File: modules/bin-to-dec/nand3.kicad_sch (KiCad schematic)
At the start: 8 parts, among them Q1 DMP3099L, Q2 DMP3099L, Q3 2N7002, Q4 2N7002, Q5 2N7002, Q6 2N7002, Q7 DMP3099L, Q8 DMP3099L

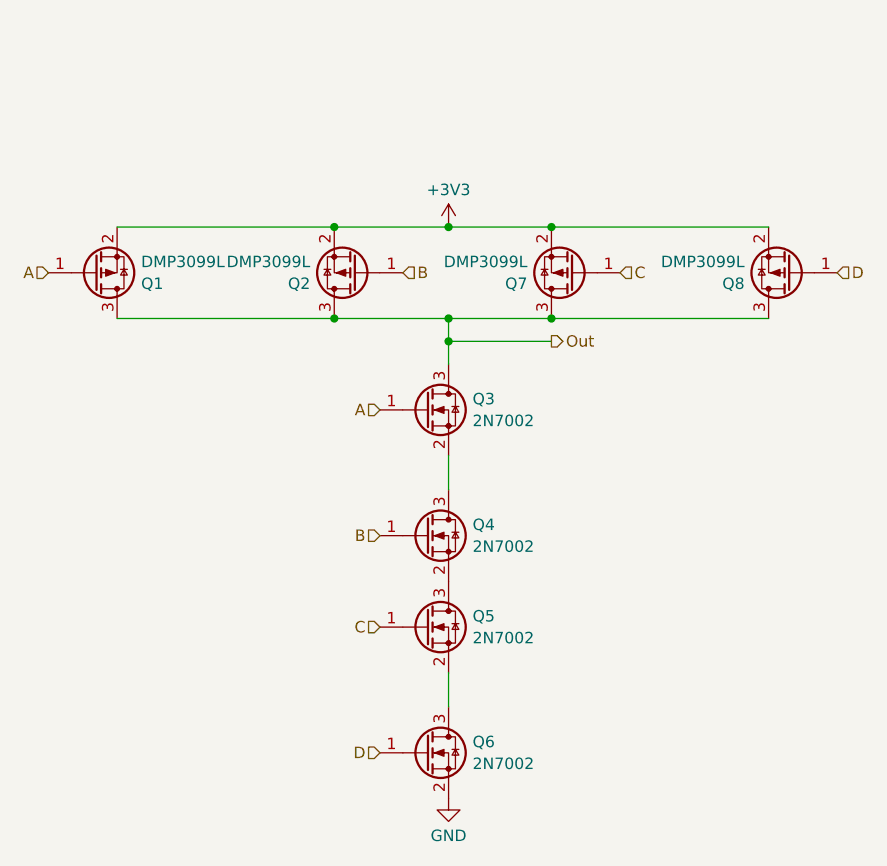
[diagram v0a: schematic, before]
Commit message: move to correct dir. improved symmetry of pcb
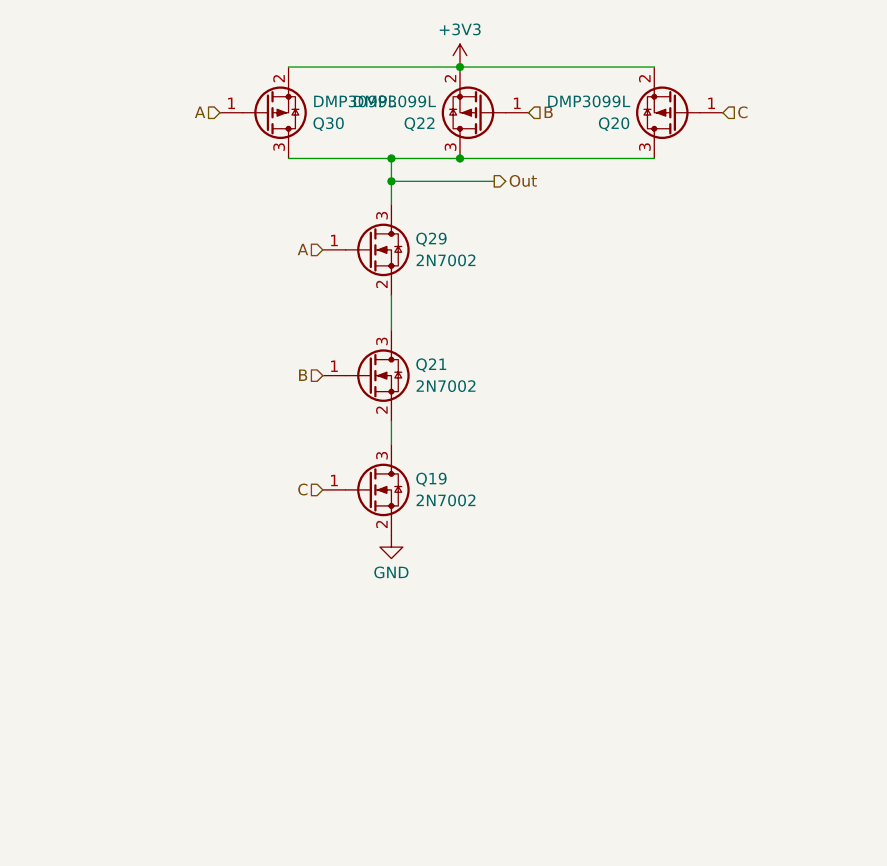
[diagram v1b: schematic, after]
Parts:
- removed Q1, Q2, Q7, Q8: DMP3099L, Package_TO_SOT_SMD:SOT-23, symbol Transistor_FET:DMP3099L
- removed Q3, Q4, Q5, Q6: 2N7002, Package_TO_SOT_SMD:SOT-23, symbol Transistor_FET:2N7002
- added Q19, Q21, Q29: 2N7002, Package_TO_SOT_SMD:SOT-23, symbol Transistor_FET:2N7002
- added Q20, Q22, Q30: DMP3099L, Package_TO_SOT_SMD:SOT-23, symbol Transistor_FET:DMP3099L
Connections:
- net +3V3: now also Q20.2 (S), Q22.2 (S), Q30.2 (S)
- net A: now also Q29.1 (G), Q30.1 (G)
- net B: now also Q21.1 (G), Q22.1 (G)
- net C: now also Q19.1 (G), Q20.1 (G)
- net GND: now also Q19.2 (S)
- net Out: now also Q20.3 (D), Q22.3 (D), Q29.3 (D), Q30.3 (D)
- new net: Q21.3 (D), Q29.2 (S)
- new net: Q19.3 (D), Q21.2 (S)

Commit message: using plugin to generate jlc production files
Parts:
- Q19, Q21, Q29: LCSC Part # (none) -> C8545
- Q20, Q22, Q30: LCSC Part # (none) -> C2940610
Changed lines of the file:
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@@
+			)
+		)
+		(property "LCSC Part #" "C8545"
+			(at 135.89 69.85 0)
+			(effects
+				(font
+					(size 1.27 1.27)
+				)
+				(hide yes)
 			)
 		)
@@
 			)
 		)
+		(property "LCSC Part #" "C8545"
+			(at 135.89 83.82 0)
+			(effects
+				(font
+					(size 1.27 1.27)
+				)
+				(hide yes)
+			)
+		)
 		(pin "1"
 		)
@@
 			)
 		)
+		(property "LCSC Part #" "C8545"
+			(at 135.89 96.52 0)
+			(effects
+				(font
+					(size 1.27 1.27)
+				)
+				(hide yes)
+			)
+		)
 		(pin "1"
 		)
@@
 			)
 		)
+		(property "LCSC Part #" "C2940610"
+			(at 124.46 54.61 0)
+			(effects
+				(font
+					(size 1.27 1.27)
+				)
+				(hide yes)
+			)
+		)
 		(pin "2"
 		)
@@
 			)
 		)
+		(property "LCSC Part #" "C2940610"
+			(at 170.18 54.61 0)
+			(effects
+				(font
+					(size 1.27 1.27)
+				)
+				(hide yes)
+			)
+		)
 		(pin "2"
 		)
@@
 			(at 148.59 54.61 0)
 			(effects
+				(font
+					(size 1.27 1.27)
+				)
+				(hide yes)
+			)
+		)
+		(property "LCSC Part #" "C2940610"
+			(at 148.59 54.61 0)
+			(effects

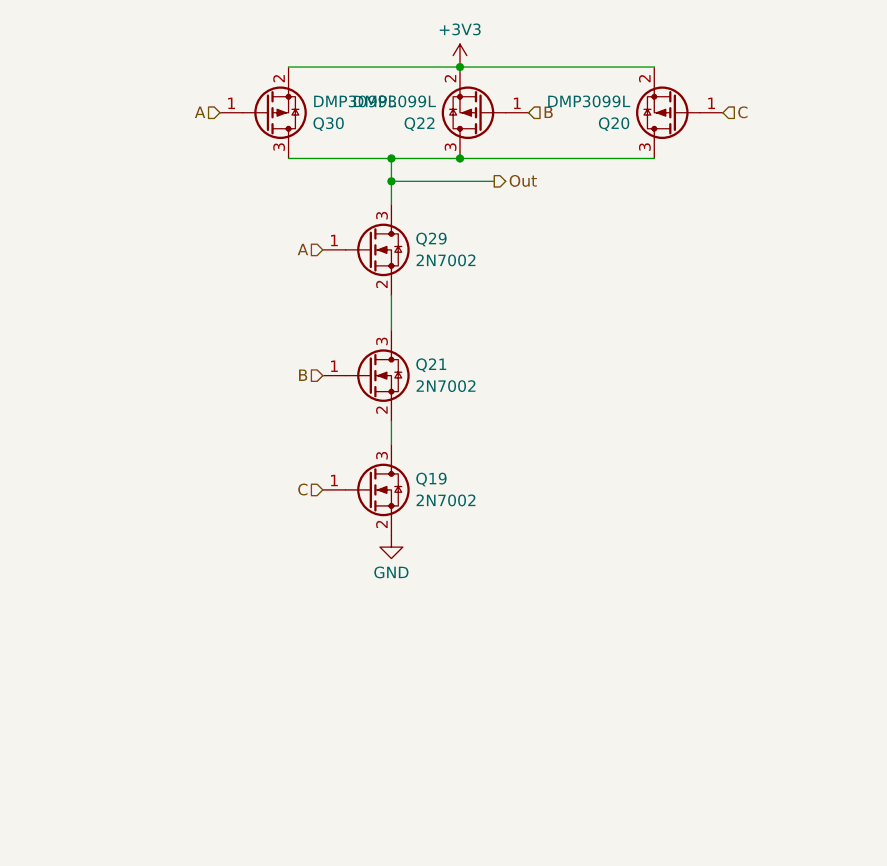
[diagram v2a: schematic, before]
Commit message: move components to top layer :(
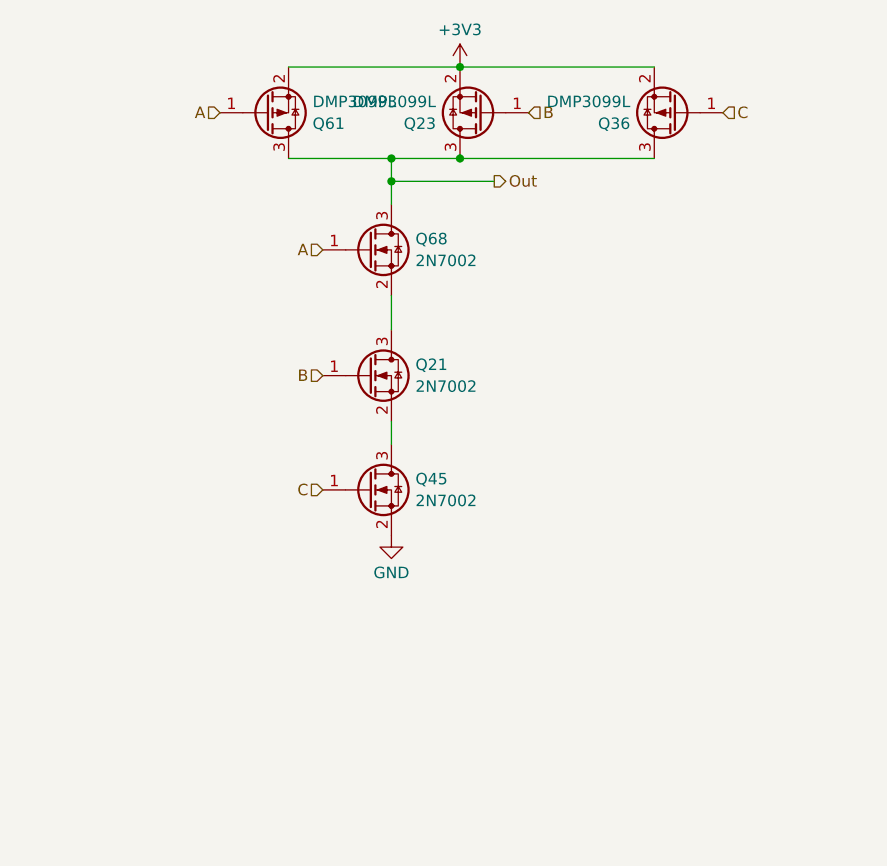
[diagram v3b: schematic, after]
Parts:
- Q21: LCSC part number (none) -> C8545
- Q23: renamed from Q22; LCSC part number (none) -> C2940610
- Q36: renamed from Q20; LCSC part number (none) -> C2940610
- Q45: renamed from Q19; LCSC part number (none) -> C8545
- Q61: renamed from Q30; LCSC part number (none) -> C2940610
- Q68: renamed from Q29; LCSC part number (none) -> C8545

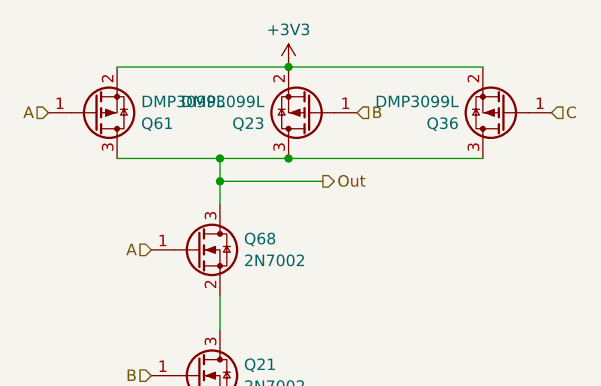
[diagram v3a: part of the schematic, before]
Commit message: switched to jlc basic components
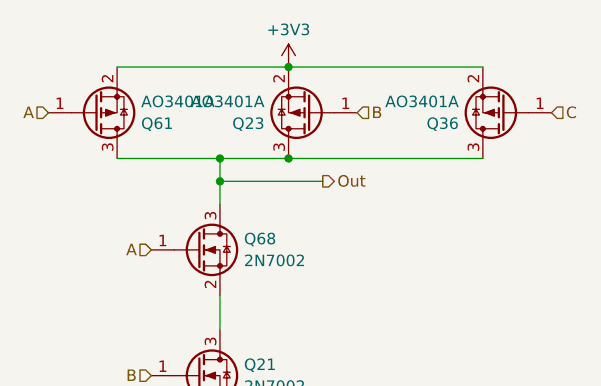
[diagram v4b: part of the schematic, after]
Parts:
- Q23, Q36, Q61: value DMP3099L -> AO3401A; LCSC Part # C2940610 -> C15127
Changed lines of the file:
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@@
 			)
 		)
-		(property "Value" "DMP3099L"
+		(property "Value" "AO3401A"
 			(at 129.667 53.3979 0)
 			(effects
@@
 			)
 		)
-		(property "Datasheet" "https://www.diodes.com/assets/Datasheets/DMP3099L.pdf"
+		(property "Datasheet" "https://jlcpcb.com/api/file/downloadByFileSystemAccessId/8553305450243108864"
 			(at 129.54 50.8 0)
 			(effects
@@
 			)
 		)
-		(property "LCSC Part #" "C2940610"
+		(property "LCSC Part #" "C15127"
 			(at 124.46 54.61 0)
 			(effects
@@
 			)
 		)
-		(property "Value" "DMP3099L"
+		(property "Value" "AO3401A"
 			(at 164.973 53.3979 0)
 			(effects
@@
 			)
 		)
-		(property "Datasheet" "https://www.diodes.com/assets/Datasheets/DMP3099L.pdf"
+		(property "Datasheet" "https://jlcpcb.com/api/file/downloadByFileSystemAccessId/8553305450243108864"
 			(at 165.1 50.8 0)
 			(effects
@@
 			)
 		)
-		(property "LCSC Part #" "C2940610"
+		(property "LCSC Part #" "C15127"
 			(at 170.18 54.61 0)
 			(effects
@@
 			)
 		)
-		(property "Value" "DMP3099L"
+		(property "Value" "AO3401A"
 			(at 143.383 53.3979 0)
 			(effects
@@
 			)
 		)
-		(property "Datasheet" "https://www.diodes.com/assets/Datasheets/DMP3099L.pdf"
+		(property "Datasheet" "https://jlcpcb.com/api/file/downloadByFileSystemAccessId/8553305450243108864"
 			(at 143.51 50.8 0)
 			(effects
@@
 			)
 		)
-		(property "LCSC Part #" "C2940610"
+		(property "LCSC Part #" "C15127"
 			(at 148.59 54.61 0)
 			(effects

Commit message: minor edits
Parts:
- Q21, Q45, Q68: LCSC part number C8545 -> (none)
- Q23, Q36, Q61: LCSC part number C2940610 -> (none)
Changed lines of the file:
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@@
-			)
-		)
-		(property "LCSC part number" "C8545"
-			(at 135.89 69.85 0)
-			(effects
-				(font
-					(size 1.27 1.27)
-				)
-				(hide yes)
 			)
 		)
@@
 			)
 		)
-		(property "LCSC part number" "C8545"
-			(at 135.89 83.82 0)
-			(effects
-				(font
-					(size 1.27 1.27)
-				)
-				(hide yes)
-			)
-		)
 		(pin "1"
 		)
@@
 			)
 		)
-		(property "LCSC part number" "C8545"
-			(at 135.89 96.52 0)
-			(effects
-				(font
-					(size 1.27 1.27)
-				)
-				(hide yes)
-			)
-		)
 		(pin "1"
 		)
@@
 			)
 		)
-		(property "LCSC part number" "C2940610"
-			(at 124.46 54.61 0)
-			(effects
-				(font
-					(size 1.27 1.27)
-				)
-				(hide yes)
-			)
-		)
 		(pin "2"
 		)
@@
 			)
 		)
-		(property "LCSC part number" "C2940610"
-			(at 170.18 54.61 0)
-			(effects
-				(font
-					(size 1.27 1.27)
-				)
-				(hide yes)
-			)
-		)
 		(pin "2"
 		)
@@
 			(at 148.59 54.61 0)
 			(effects
-				(font
-					(size 1.27 1.27)
-				)
-				(hide yes)
-			)
-		)
-		(property "LCSC part number" "C2940610"
-			(at 148.59 54.61 0)
-			(effects
